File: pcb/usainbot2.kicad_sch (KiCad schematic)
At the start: 21 parts, among them J1 BT_MOD, J2 QTR1-L, J3 QTR1-R, J4 QTR-6A, J5 M1, J6 BATT, J7 M2, SW1 SW_SPDT, SW2 SW_Push, U1 TB6612FNG_breakout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

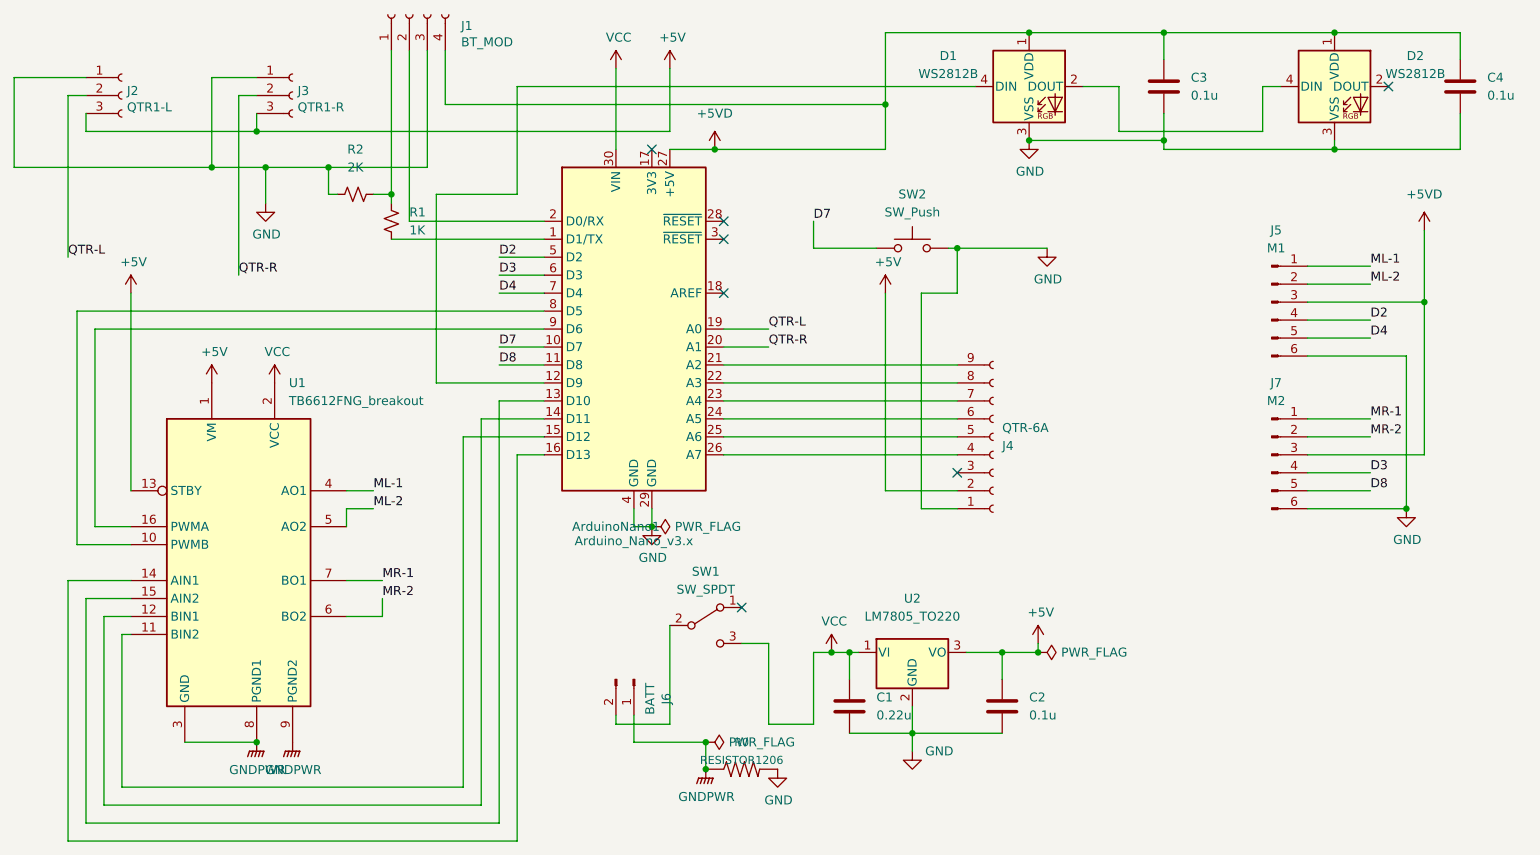
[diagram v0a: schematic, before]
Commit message: corrige error de diseño
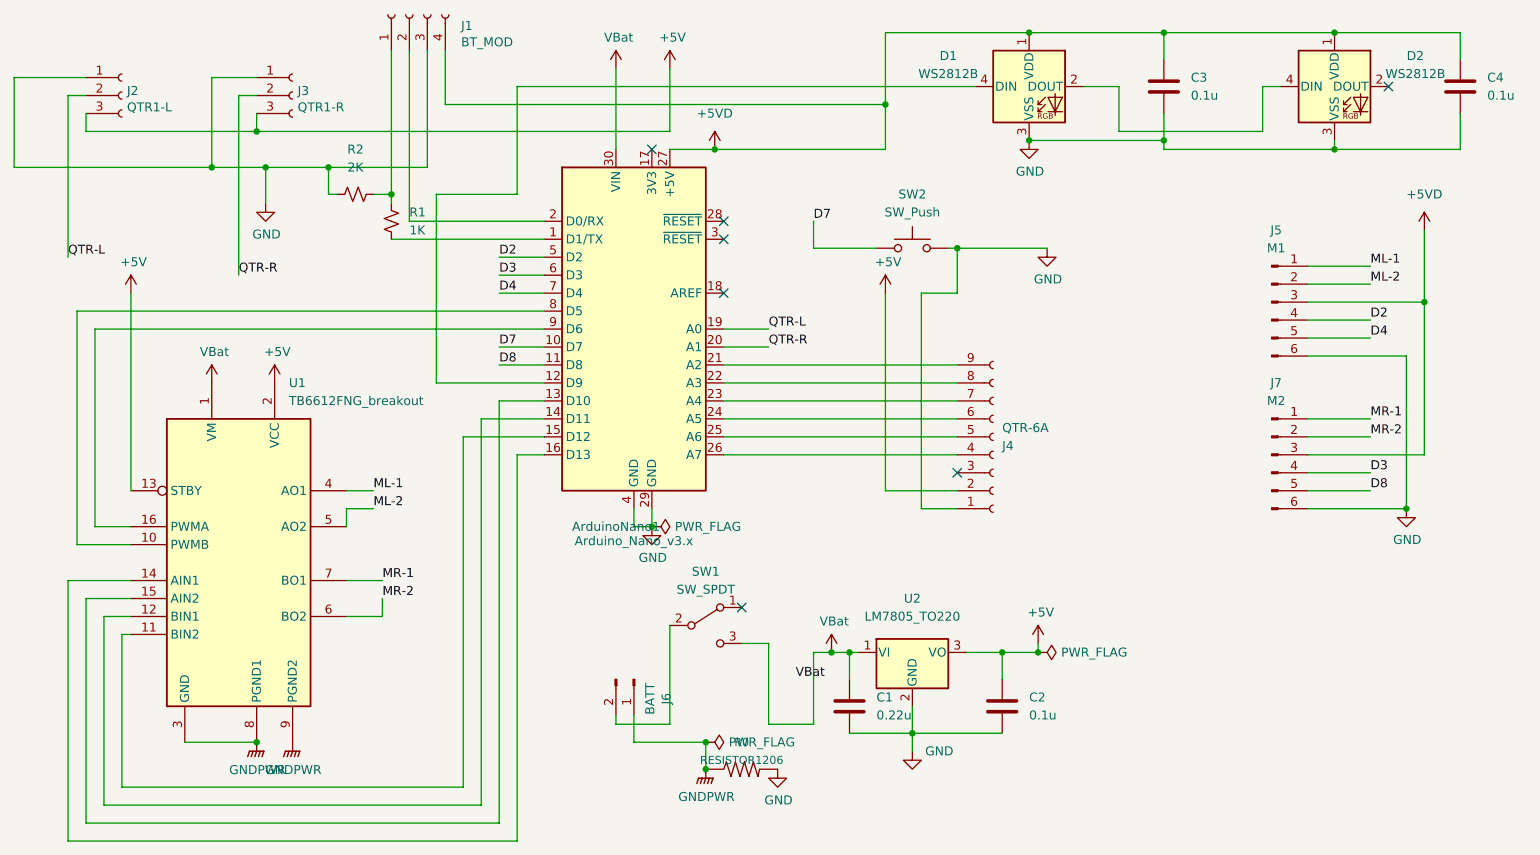
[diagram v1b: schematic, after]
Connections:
- net +5V: now also U1.2 (VCC); no longer U1.1 (VM)
- net VCC: now also U1.1 (VM); no longer U1.2 (VCC)
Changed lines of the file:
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@@
+    (effects (font (size 1.27 1.27)) (justify left bottom))
+  )
+  (label "VBat" (at 152.4 127 0)
     (effects (font (size 1.27 1.27)) (justify left bottom))
   )
@@
       (effects (font (size 1.27 1.27)) hide)
     )
-    (property "Value" "VCC" (id 1) (at 127.381 36.2458 0))
+    (property "Value" "VBat" (id 1) (at 127.381 36.2458 0))
     (property "Footprint" "" (id 2) (at 127 40.64 0)
       (effects (font (size 1.27 1.27)) hide)
@@
     (pin "1")
   )
-  (symbol (lib_id "usainbot2-rescue:+5V-power") (at 69.85 85.09 0) (unit 1)
-    (in_bom yes) (on_board yes)
-    (property "Reference" "#PWR0107" (id 0) (at 69.85 88.9 0)
-      (effects (font (size 1.27 1.27)) hide)
-    )
-    (property "Value" "+5V" (id 1) (at 70.231 80.6958 0))
-    (property "Footprint" "" (id 2) (at 69.85 85.09 0)
-      (effects (font (size 1.27 1.27)) hide)
-    )
-    (property "Datasheet" "" (id 3) (at 69.85 85.09 0)
+  (symbol (lib_id "usainbot2-rescue:+5V-power") (at 78.74 85.09 0) (unit 1)
+    (in_bom yes) (on_board yes)
+    (property "Reference" "#PWR0107" (id 0) (at 78.74 88.9 0)
+      (effects (font (size 1.27 1.27)) hide)
+    )
+    (property "Value" "+5V" (id 1) (at 79.121 80.6958 0))
+    (property "Footprint" "" (id 2) (at 78.74 85.09 0)
+      (effects (font (size 1.27 1.27)) hide)
+    )
+    (property "Datasheet" "" (id 3) (at 78.74 85.09 0)
       (effects (font (size 1.27 1.27)) hide)
     )
@@
     (pin "1")
   )
-  (symbol (lib_id "usainbot2-rescue:VCC-power") (at 78.74 85.09 0) (unit 1)
-    (in_bom yes) (on_board yes)
-    (property "Reference" "#PWR0112" (id 0) (at 78.74 88.9 0)
-      (effects (font (size 1.27 1.27)) hide)
-    )
-    (property "Value" "VCC" (id 1) (at 79.121 80.6958 0))
-    (property "Footprint" "" (id 2) (at 78.74 85.09 0)
-      (effects (font (size 1.27 1.27)) hide)
-    )
-    (property "Datasheet" "" (id 3) (at 78.74 85.09 0)
+  (symbol (lib_id "usainbot2-rescue:VCC-power") (at 69.85 85.09 0) (unit 1)
+    (in_bom yes) (on_board yes)
+    (property "Reference" "#PWR0112" (id 0) (at 69.85 88.9 0)
+      (effects (font (size 1.27 1.27)) hide)
+    )
+    (property "Value" "VBat" (id 1) (at 70.231 80.6958 0))
+    (property "Footprint" "" (id 2) (at 69.85 85.09 0)
+      (effects (font (size 1.27 1.27)) hide)
+    )
+    (property "Datasheet" "" (id 3) (at 69.85 85.09 0)
       (effects (font (size 1.27 1.27)) hide)
     )
@@
       (effects (font (size 1.27 1.27)) hide)
     )
-    (property "Value" "VCC" (id 1) (at 157.861 118.7958 0))
+    (property "Value" "VBat" (id 1) (at 157.861 118.7958 0))
     (property "Footprint" "" (id 2) (at 157.48 123.19 0)
       (effects (font (size 1.27 1.27)) hide)
@@
     )
     (path "/00000000-0000-0000-0000-00006246b70d"
-      (reference "#PWR0103") (unit 1) (value "VCC") (footprint "")
+      (reference "#PWR0103") (unit 1) (value "VBat") (footprint "")
     )
     (path "/0fbe4066-40a9-4e86-906d-3aef413a81c3"
@@
     )
     (path "/00000000-0000-0000-0000-0000624a088e"
-      (reference "#PWR0112") (unit 1) (value "VCC") (footprint "")
+      (reference "#PWR0112") (unit 1) (value "VBat") (footprint "")
     )
     (path "/da89e122-b44a-433a-86d6-892de8bfb068"
@@
     )
     (path "/2edaf02e-db08-4ad9-80c3-995b7477369f"
-      (reference "#PWR0116") (unit 1) (value "VCC") (footprint "")
+      (reference "#PWR0116") (unit 1) (value "VBat") (footprint "")
     )
     (path "/2f62211a-1e2a-40b1-85f4-91f214ecd7e5"
